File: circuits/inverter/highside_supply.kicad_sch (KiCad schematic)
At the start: 37 parts

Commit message: converts libraries to Kicad 6 format, updates bridge driver
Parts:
- gave numbers to parts that had none: 6

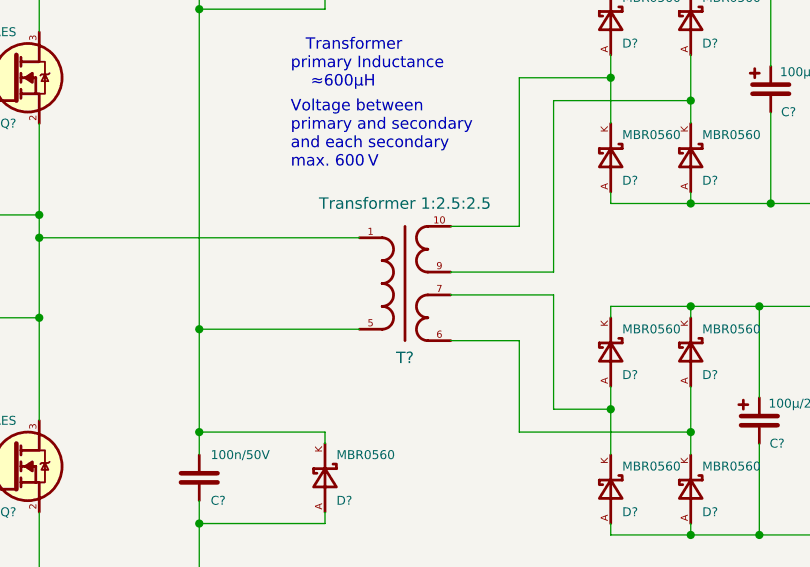
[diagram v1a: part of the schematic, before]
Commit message: converts the project to Kicad 7
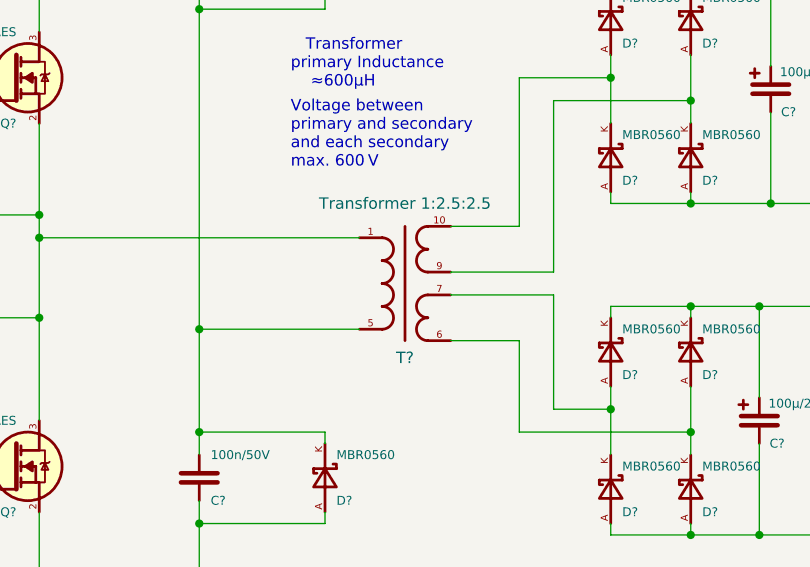
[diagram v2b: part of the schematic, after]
